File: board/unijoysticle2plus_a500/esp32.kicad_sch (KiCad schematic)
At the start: 17 parts, among them SW1 RESET, SW3 BOOT, U4 ESP32-WROOM-32E

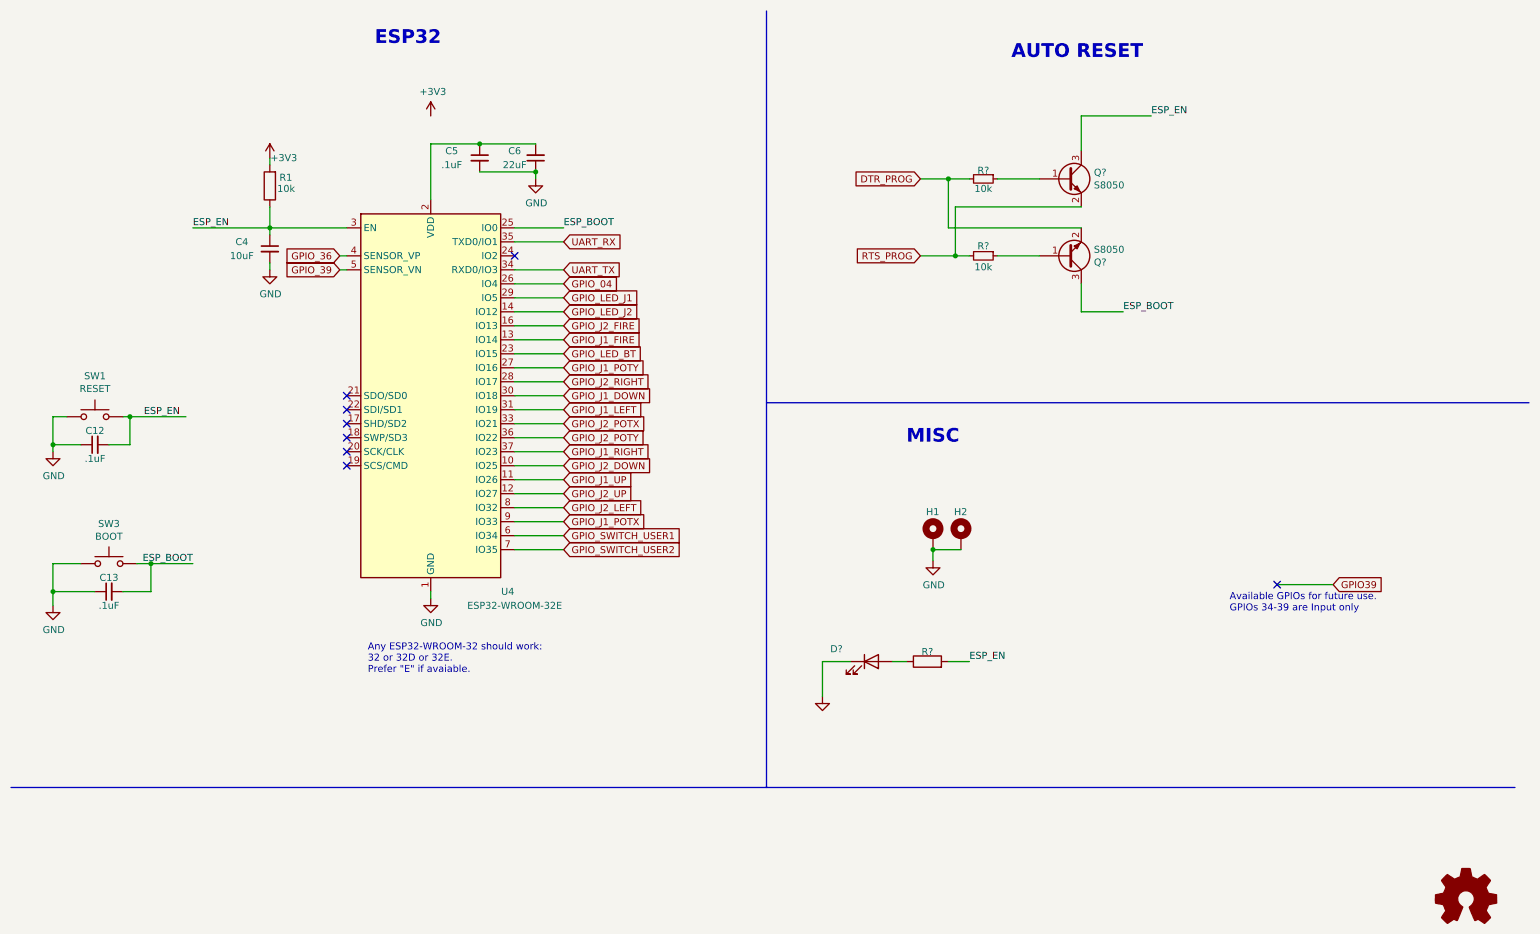
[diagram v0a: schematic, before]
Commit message: a500: remove duplicate symbols
It is able to run the EDR checks with 5 warnings.
Only one looks worth taking a look at.
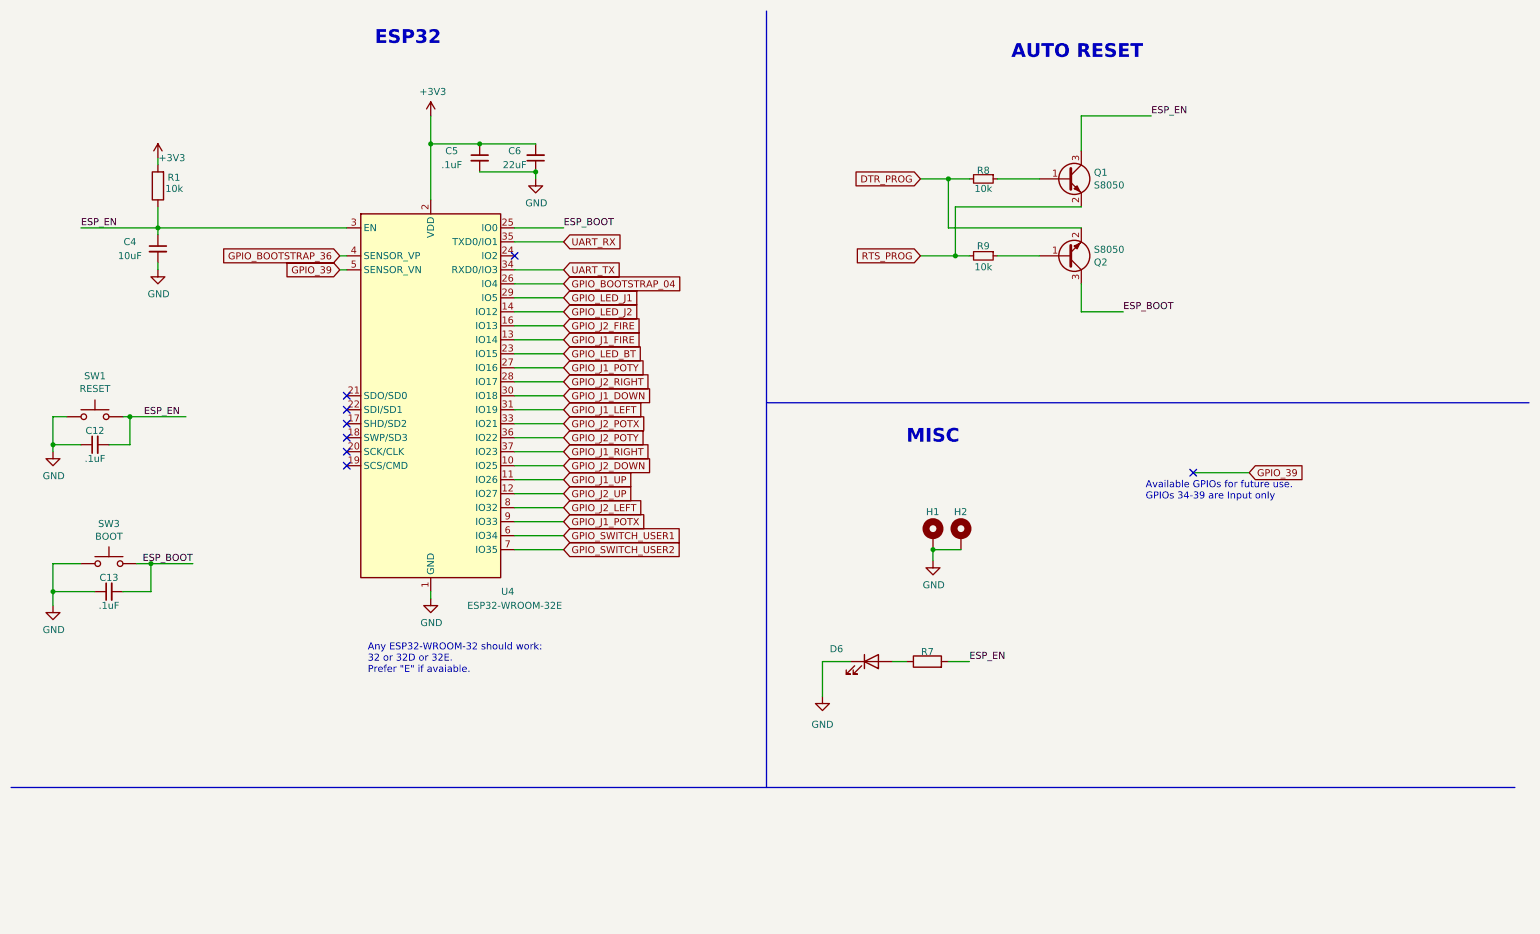
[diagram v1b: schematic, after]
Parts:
- gave numbers to parts that had none: 6
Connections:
- net +3V3: now also C5.1, C6.2, U4.2 (VDD)
- net GPIO_04 renamed GPIO_BOOTSTRAP_04
- net GPIO_36 renamed GPIO_BOOTSTRAP_36
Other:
- moved on the sheet: C4, R1

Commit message: uni2+ a500: schematic "ready"
The schematic should be "ready".
Layout WIP. Components were placed in "place".
But routing is missing, as well as logos
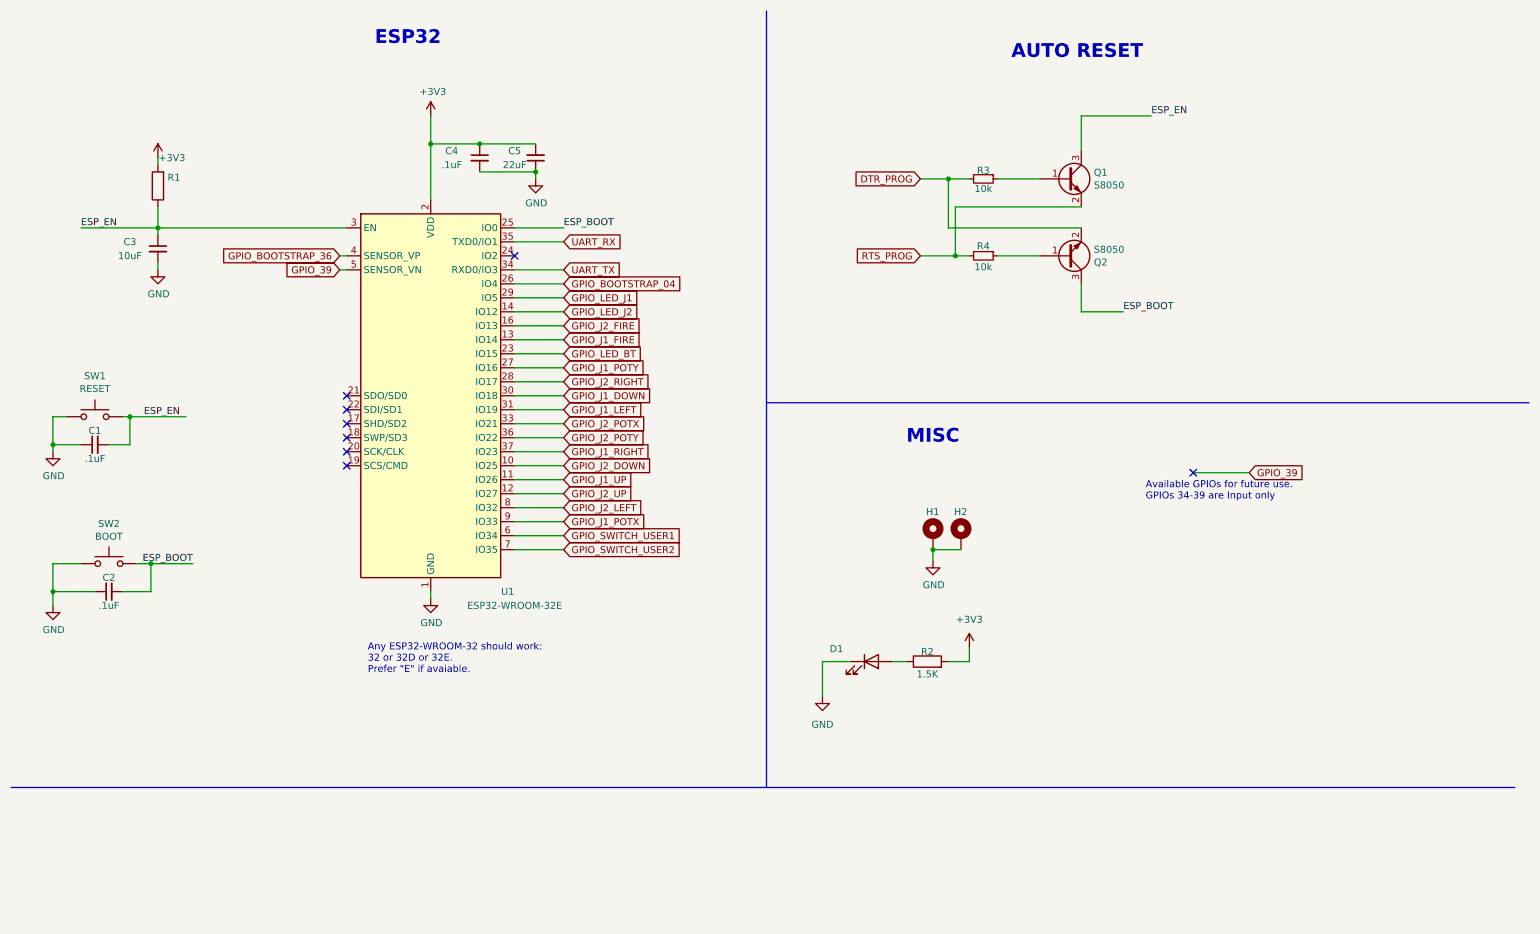
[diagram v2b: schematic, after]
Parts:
- D1: renamed from D6; value ~ -> (none)
- R1: value 10k -> (none); footprint Resistor_SMD:R_0805_2012Metric_Pad1.20x1.40mm_HandSolder -> (none)
- R2: renamed from R7; value ~ -> 1.5K; footprint (none) -> Resistor_SMD:R_0805_2012Metric_Pad1.20x1.40mm_HandSolder
- renumbered C12 to C1, C13 to C2, C4 to C3, C5 to C4, C6 to C5, R8 to R3, R9 to R4, SW3 to SW2, U4 to U1
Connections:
- net +3V3: now also R2.2
- net ESP_EN: no longer R2.2
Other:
- title: Unijoysticle 2+ -> Unijoysticle 2+ A500
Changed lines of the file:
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@@
   (paper "A4")
   (title_block
-    (title "Unijoysticle 2+")
-    (date "2022-01-02")
-    (rev "H")
+    (title "Unijoysticle 2+ A500")
+    (date "2022-04-20")
+    (rev "A")
     (company "Retro Moe")
   )
@@
     (stroke (width 0) (type default) (color 0 0 0 0))
   )
+  (wire (pts (xy 185.42 128.27) (xy 185.42 130.81))
+    (stroke (width 0) (type default) (color 0 0 0 0))
+  )
   (wire (pts (xy 102.87 67.31) (xy 111.76 67.31))
     (stroke (width 0) (type default) (color 0 0 0 0))
@@
   )
   (label "ESP_EN" (at 35.56 86.36 0)
-    (effects (font (size 1.27 1.27)) (justify left bottom))
-  )
-  (label "ESP_EN" (at 185.42 130.81 0)
     (effects (font (size 1.27 1.27)) (justify left bottom))
   )
@@
   (symbol (lib_id "RF_Module:ESP32-WROOM-32D") (at 87.63 82.55 0) (unit 1)
     (in_bom yes) (on_board yes)
-    (property "Reference" "U4" (id 0) (at 101.6 118.11 0))
+    (property "Reference" "U1" (id 0) (at 101.6 118.11 0))
     (property "Value" "ESP32-WROOM-32E" (id 1) (at 102.87 120.65 0))
     (property "Footprint" "RF_Module:ESP32-WROOM-32" (id 2) (at 87.63 120.65 0)
@@
   (symbol (lib_id "power:GND") (at 87.63 119.38 0) (unit 1)
     (in_bom yes) (on_board yes)
-    (property "Reference" "#PWR016" (id 0) (at 87.63 125.73 0)
+    (property "Reference" "#PWR06" (id 0) (at 87.63 125.73 0)
       (effects (font (size 1.27 1.27)) hide)
     )
@@
       (effects (font (size 1.27 1.27)) (justify left))
     )
-    (property "Value" "10k" (id 1) (at 42.672 44.958 0)
+    (property "Value" "" (id 1) (at 42.672 44.958 0)
       (effects (font (size 1.27 1.27)) (justify left))
     )
-    (property "Footprint" "Resistor_SMD:R_0805_2012Metric_Pad1.20x1.40mm_HandSolder" (id 2) (at 39.878 44.45 90)
+    (property "Footprint" "" (id 2) (at 39.878 44.45 90)
       (effects (font (size 1.27 1.27)) hide)
     )
@@
   (symbol (lib_id "power:+3V3") (at 38.1 39.37 0) (unit 1)
     (in_bom yes) (on_board yes)
-    (property "Reference" "#PWR013" (id 0) (at 38.1 43.18 0)
+    (property "Reference" "#PWR03" (id 0) (at 38.1 43.18 0)
       (effects (font (size 1.27 1.27)) hide)
     )
@@
   (symbol (lib_id "power:GND") (at 38.1 59.69 0) (unit 1)
     (in_bom yes) (on_board yes)
-    (property "Reference" "#PWR010" (id 0) (at 38.1 66.04 0)
+    (property "Reference" "#PWR04" (id 0) (at 38.1 66.04 0)
       (effects (font (size 1.27 1.27)) hide)
     )
@@
   (symbol (lib_id "power:+3V3") (at 87.63 31.75 0) (unit 1)
     (in_bom yes) (on_board yes)
-    (property "Reference" "#PWR015" (id 0) (at 87.63 35.56 0)
+    (property "Reference" "#PWR05" (id 0) (at 87.63 35.56 0)
       (effects (font (size 1.27 1.27)) hide)
     )
@@
   (symbol (lib_id "power:GND") (at 19.05 92.71 0) (unit 1)
     (in_bom yes) (on_board yes)
-    (property "Reference" "#PWR09" (id 0) (at 19.05 99.06 0)
+    (property "Reference" "#PWR01" (id 0) (at 19.05 99.06 0)
       (effects (font (size 1.27 1.27)) hide)
     )
@@
   (symbol (lib_id "Device:C_Small") (at 26.67 91.44 90) (unit 1)
     (in_bom yes) (on_board yes)
-    (property "Reference" "C12" (id 0) (at 26.67 88.9 90))
+    (property "Reference" "C1" (id 0) (at 26.67 88.9 90))
     (property "Value" ".1uF" (id 1) (at 26.67 93.98 90))
     (property "Footprint" "Capacitor_SMD:C_0805_2012Metric_Pad1.18x1.45mm_HandSolder" (id 2) (at 26.67 91.44 0)
@@
   (symbol (lib_id "power:GND") (at 178.816 112.522 0) (unit 1)
     (in_bom yes) (on_board yes)
-    (property "Reference" "#PWR0104" (id 0) (at 178.816 118.872 0)
+    (property "Reference" "#PWR09" (id 0) (at 178.816 118.872 0)
       (effects (font (size 1.27 1.27)) hide)
     )
@@
   (symbol (lib_id "Device:C_Small") (at 38.1 55.88 0) (unit 1)
     (in_bom yes) (on_board yes)
-    (property "Reference" "C4" (id 0) (at 33.02 54.61 0))
+    (property "Reference" "C3" (id 0) (at 33.02 54.61 0))
     (property "Value" "10uF" (id 1) (at 33.02 57.15 0))
     (property "Footprint" "Capacitor_SMD:C_0805_2012Metric_Pad1.18x1.45mm_HandSolder" (id 2) (at 38.1 55.88 0)
@@
   (symbol (lib_id "power:GND") (at 106.68 43.18 0) (unit 1)
     (in_bom yes) (on_board yes)
-    (property "Reference" "#PWR0114" (id 0) (at 106.68 49.53 0)
+    (property "Reference" "#PWR07" (id 0) (at 106.68 49.53 0)
       (effects (font (size 1.27 1.27)) hide)
     )
@@
   (symbol (lib_id "Switch:SW_Push") (at 29.21 113.03 0) (unit 1)
     (in_bom yes) (on_board yes)
-    (property "Reference" "SW3" (id 0) (at 29.21 105.791 0))
+    (property "Reference" "SW2" (id 0) (at 29.21 105.791 0))
     (property "Value" "BOOT" (id 1) (at 29.21 108.1024 0))
     (property "Footprint" "Unijoysticle:SW_Push_1P1T_NO_5.1x5.1mm" (id 2) (at 29.21 107.95 0)
@@
   (symbol (lib_id "power:GND") (at 19.05 120.65 0) (unit 1)
     (in_bom yes) (on_board yes)
-    (property "Reference" "#PWR0108" (id 0) (at 19.05 127 0)
+    (property "Reference" "#PWR02" (id 0) (at 19.05 127 0)
       (effects (font (size 1.27 1.27)) hide)
     )
@@
   (symbol (lib_id "Device:C_Small") (at 29.21 118.11 90) (unit 1)
     (in_bom yes) (on_board yes)
-    (property "Reference" "C13" (id 0) (at 29.21 115.57 90))
+    (property "Reference" "C2" (id 0) (at 29.21 115.57 90))
     (property "Value" ".1uF" (id 1) (at 29.21 120.65 90))
     (property "Footprint" "Capacitor_SMD:C_0805_2012Metric_Pad1.18x1.45mm_HandSolder" (id 2) (at 29.21 118.11 0)
@@
   (symbol (lib_id "Device:C_Small") (at 106.68 39.37 180) (unit 1)
     (in_bom yes) (on_board yes)
-    (property "Reference" "C6" (id 0) (at 102.87 38.1 0))
+    (property "Reference" "C5" (id 0) (at 102.87 38.1 0))
     (property "Value" "22uF" (id 1) (at 102.87 40.64 0))
     (property "Footprint" "Capacitor_SMD:C_0805_2012Metric_Pad1.18x1.45mm_HandSolder" (id 2) (at 106.68 39.37 0)
@@
   (symbol (lib_id "Device:C_Small") (at 96.52 39.37 0) (unit 1)
     (in_bom yes) (on_board yes)
-    (property "Reference" "C5" (id 0) (at 91.44 38.1 0))
+    (property "Reference" "C4" (id 0) (at 91.44 38.1 0))
     (property "Value" ".1uF" (id 1) (at 91.44 40.64 0))
     (property "Footprint" "Capacitor_SMD:C_0805_2012Metric_Pad1.18x1.45mm_HandSolder" (id 2) (at 96.52 39.37 0)
@@
     (pin "2")
   )
+  (symbol (lib_id "power:+3V3") (at 185.42 128.27 0) (unit 1)
+    (in_bom yes) (on_board yes) (fields_autoplaced)
+    (property "Reference" "#PWR010" (id 0) (at 185.42 132.08 0)
+      (effects (font (size 1.27 1.27)) hide)
+    )
+    (property "Value" "+3V3" (id 1) (at 185.42 123.19 0))
+    (property "Footprint" "" (id 2) (at 185.42 128.27 0)
+      (effects (font (size 1.27 1.27)) hide)
+    )
+    (property "Datasheet" "" (id 3) (at 185.42 128.27 0)
+      (effects (font (size 1.27 1.27)) hide)
+    )
+    (pin "1")
+  )
   (symbol (lib_id "power:GND") (at 158.75 137.16 0) (unit 1)
     (in_bom yes) (on_board yes) (fields_autoplaced)
-    (property "Reference" "#PWR01" (id 0) (at 158.75 143.51 0)
+    (property "Reference" "#PWR08" (id 0) (at 158.75 143.51 0)
       (effects (font (size 1.27 1.27)) hide)
     )
@@
   (symbol (lib_id "Device:R_Small") (at 187.96 43.18 270) (unit 1)
     (in_bom yes) (on_board yes)
-    (property "Reference" "R8" (id 0) (at 187.96 41.656 90))
+    (property "Reference" "R3" (id 0) (at 187.96 41.656 90))
     (property "Value" "10k" (id 1) (at 187.96 44.958 90))
     (property "Footprint" "Resistor_SMD:R_0805_2012Metric_Pad1.20x1.40mm_HandSolder" (id 2) (at 187.96 43.18 0)
@@
   (symbol (lib_id "Device:LED") (at 167.64 130.81 0) (unit 1)
     (in_bom yes) (on_board yes)
-    (property "Reference" "D6" (id 0) (at 161.29 128.524 0))
-    (property "Value" "~" (id 1) (at 167.64 128.524 0))
+    (property "Reference" "D1" (id 0) (at 161.29 128.524 0))
+    (property "Value" "" (id 1) (at 167.64 128.524 0))
     (property "Footprint" "" (id 2) (at 167.64 130.81 0)
       (effects (font (size 1.27 1.27)) hide)
@@
   (symbol (lib_id "Device:R_Small") (at 187.96 57.15 270) (unit 1)
     (in_bom yes) (on_board yes)
-    (property "Reference" "R9" (id 0) (at 187.96 55.372 90))
+    (property "Reference" "R4" (id 0) (at 187.96 55.372 90))
     (property "Value" "10k" (id 1) (at 187.96 59.182 90))
     (property "Footprint" "Resistor_SMD:R_0805_2012Metric_Pad1.20x1.40mm_HandSolder" (id 2) (at 187.96 57.15 0)
@@
   (symbol (lib_id "Device:R") (at 177.8 130.81 90) (unit 1)
     (in_bom yes) (on_board yes)
-    (property "Reference" "R7" (id 0) (at 177.8 129.032 90))
-    (property "Value" "~" (id 1) (at 177.8 133.096 90))
-    (property "Footprint" "" (id 2) (at 177.8 132.588 90)
-      (effects (font (size 1.27 1.27)) hide)
-    )
+    (property "Reference" "R2" (id 0) (at 177.8 129.032 90))
+    (property "Value" "1.5K" (id 1) (at 177.8 133.096 90))
+    (property "Footprint" "Resistor_SMD:R_0805_2012Metric_Pad1.20x1.40mm_HandSolder" (id 2) (at 177.8 132.588 90)
+      (effects (font (size 1.27 1.27)) hide)
+    )
